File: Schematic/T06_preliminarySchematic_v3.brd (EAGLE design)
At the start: 100 x 80 mm, 58 parts, among them Q3 2n3904, U1 ATMEGA328P_PDIP, X1 SSW-105-02-S-S, X2 SSW-102-02-S-S

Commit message: still trying to figutr out git
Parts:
- CSTCE16M0V53-R0: device adafruit:CERM_OSC -> adafruit:CSTCR-G
- moved SONAR2 120.9 mm to (49.5, 39.4), turned to 270 degrees
- moved R7 117.4 mm to (27.9, 2.54), turned to 270 degrees
- moved SONAR1 111.2 mm to (54.6, 39.4), turned to 270 degrees
- moved TP26 111.1 mm to (24.1, 8.89), turned to 90 degrees
- moved MOTOR2 109.8 mm to (52.1, 74.9), turned to 270 degrees
- moved R2 107.1 mm to (41.9, 3.81), turned to 90 degrees
- moved R1 106.7 mm to (29.2, 47.0)
- moved NCP1117DT33T5GOSTR-ND 105.9 mm to (33.0, 20.3)
- moved TP27 105.5 mm to (38.1, 74.9), turned to 90 degrees
- moved R5 103.1 mm to (40.6, 69.8), turned to 270 degrees
- moved TP15 99.9 mm to (27.9, 59.7), turned to 180 degrees
- moved TP16 99.5 mm to (22.9, 63.5), turned to 270 degrees
- moved MOTOR1 95.8 mm to (45.7, 74.9), turned to 270 degrees
- moved LED3 95.6 mm to (21.6, 2.54)
- moved TP2 95.2 mm to (3.81, 29.2), turned to 90 degrees
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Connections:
- net GND: now also CSTCE16M0V53-R0.2; no longer CSTCE16M0V53-R0.P$2
- net N$1: now also CSTCE16M0V53-R0.3; no longer CSTCE16M0V53-R0.P$3
- net N$2: now also CSTCE16M0V53-R0.1; no longer CSTCE16M0V53-R0.P$1

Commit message: practice makes perfect
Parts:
- removed MOTOR1, MOTOR2: SSW-102-02-S-S, con-samtec:SSW-102-02-S-S
- removed SONAR1, SONAR3: SSW-104-02-S-S, con-samtec:SSW-104-02-S-S
- removed TP15: TPPAD1-13, testpad:P1-13
- added M1, M2: SSW-102-02-S-S, con-samtec:SSW-102-02-S-S
- added S1, S3: SSW-104-02-S-S, con-samtec:SSW-104-02-S-S
- moved R5 7.62 mm to (33.0, 69.8)
- moved TP10 4.58 mm to (21.6, 29.2)
- moved TP11 4.58 mm to (21.6, 33.0)
- moved TP22 4.58 mm to (21.6, 40.6)
- moved TP7 4.58 mm to (21.6, 17.8)
- moved TP8 4.58 mm to (21.6, 21.6)
- moved TP9 4.58 mm to (21.6, 25.4)
- moved TP24 4.58 mm to (21.6, 36.8)
- moved R3 3.70 mm to (21.0, 73.0)
- moved LED2 3.42 mm to (16.5, 73.0)
- moved LED1 3.24 mm to (12.1, 73.0)
- moved TP23 3.24 mm to (3.17, 75.6), turned to 180 degrees
- moved TP26 2.69 mm to (22.2, 10.8)
- moved TP18 2.54 mm to (3.81, 66.0), turned to 180 degrees
- moved X2 2.54 mm to (12.7, 5.08)
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- renumbered CSTCE16M0V53-R0 to CSC, SONAR2 to S2
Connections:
- net +5V: now also S1.4, S3.4; no longer SONAR1.4, SONAR3.4
- net ECHO1: now also S1.2; no longer SONAR1.2
- net ECHO3: now also S3.2; no longer SONAR3.2, TP15.TP
- net GND: now also S1.1, S3.1; no longer SONAR1.1, SONAR3.1
- net N$11: now also M1.2, M2.2; no longer MOTOR1.2, MOTOR2.2
- net N$5: now also M1.1, M2.1; no longer MOTOR1.1, MOTOR2.1
- net TRIG: now also S1.3, S3.3; no longer SONAR1.3, SONAR3.3

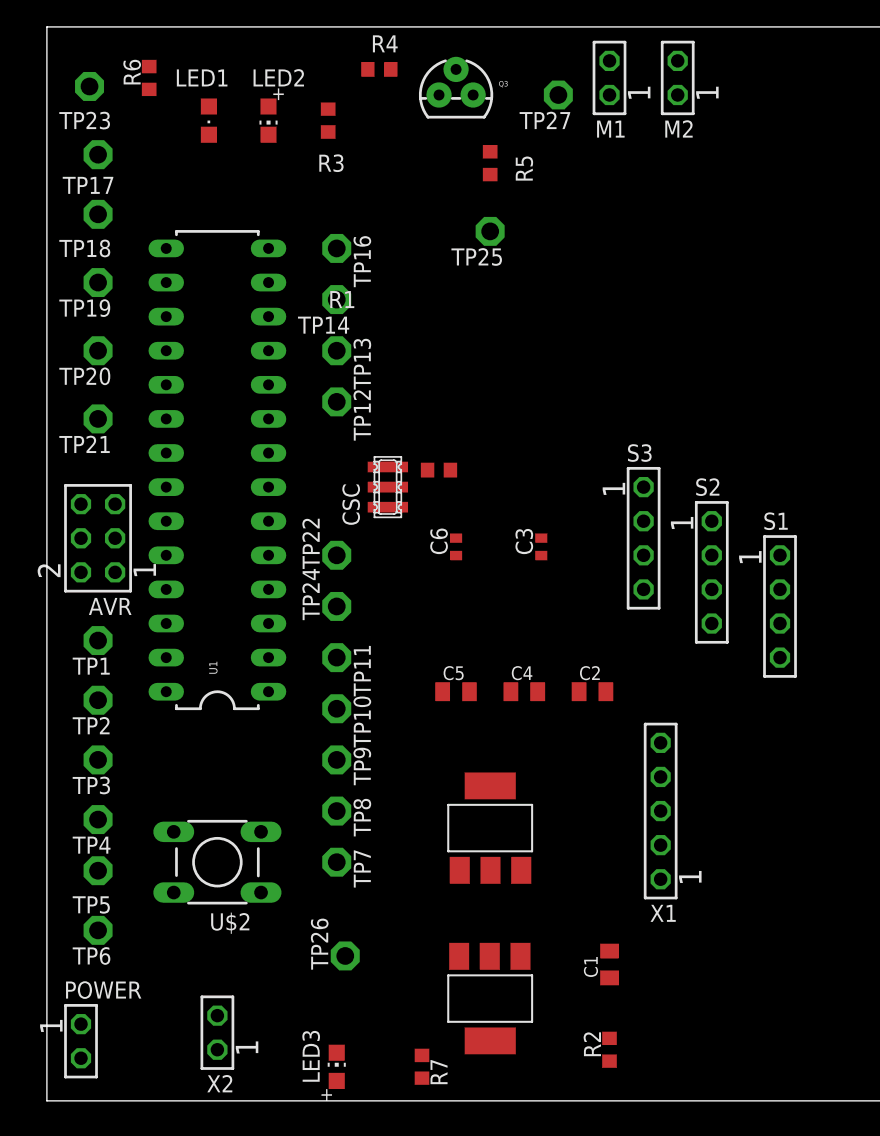
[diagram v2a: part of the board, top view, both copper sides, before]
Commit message: board done and routed, managed to do with only 1 via and no air wires
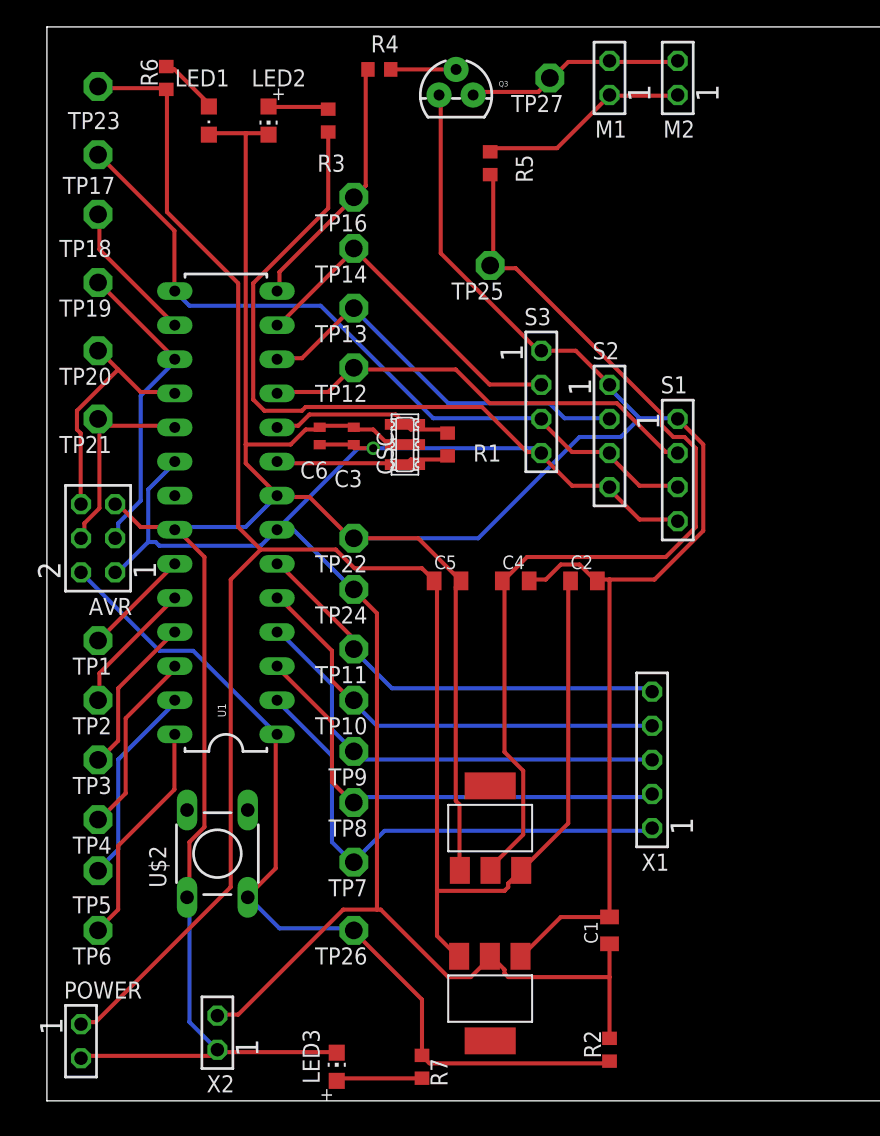
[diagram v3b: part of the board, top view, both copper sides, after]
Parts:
- moved C3 16.2 mm to (22.9, 49.5)
- moved C6 13.1 mm to (20.3, 49.5)
- moved S2 12.7 mm to (41.9, 49.5)
- moved S3 12.7 mm to (36.8, 52.1)
- moved S1 12.7 mm to (47.0, 47.0)
- moved C2 8.28 mm to (40.0, 38.7)
- moved C4 8.28 mm to (34.9, 38.7)
- moved C5 8.28 mm to (29.8, 38.7)
- moved TP14 4.02 mm to (22.9, 63.5)
- moved TP16 4.02 mm to (22.9, 67.3), turned to 180 degrees
- moved X1 3.86 mm to (45.1, 25.4)
- moved CSC 3.42 mm to (26.7, 48.9)
- moved TP13 3.42 mm to (22.9, 59.1), turned to 180 degrees
- moved U1 3.24 mm to (13.3, 43.8)
- moved TP12 2.84 mm to (22.9, 54.6), turned to 180 degrees
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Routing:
- net GND: track 0.00 -> 275.7 mm
- net +5V: track 0.00 -> 180.6 mm, vias 0 -> 1
- net +9V: track 0.00 -> 156.6 mm
- net +3V3: track 0.00 -> 73.7 mm
- net RESET: track 0.00 -> 67.3 mm
- net TRIG: track 0.00 -> 56.3 mm
- net BU0: track 0.00 -> 37.8 mm
- net BU1: track 0.00 -> 35.1 mm
- net BU2: track 0.00 -> 33.8 mm
- net ECHO1: track 0.00 -> 33.3 mm
- net BU3: track 0.00 -> 33.3 mm
- net BU4: track 0.00 -> 32.4 mm
- net ECHO2: track 0.00 -> 29.8 mm
- net ECHO3: track 0.00 -> 26.3 mm
- net MOSI: track 0.00 -> 23.4 mm
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
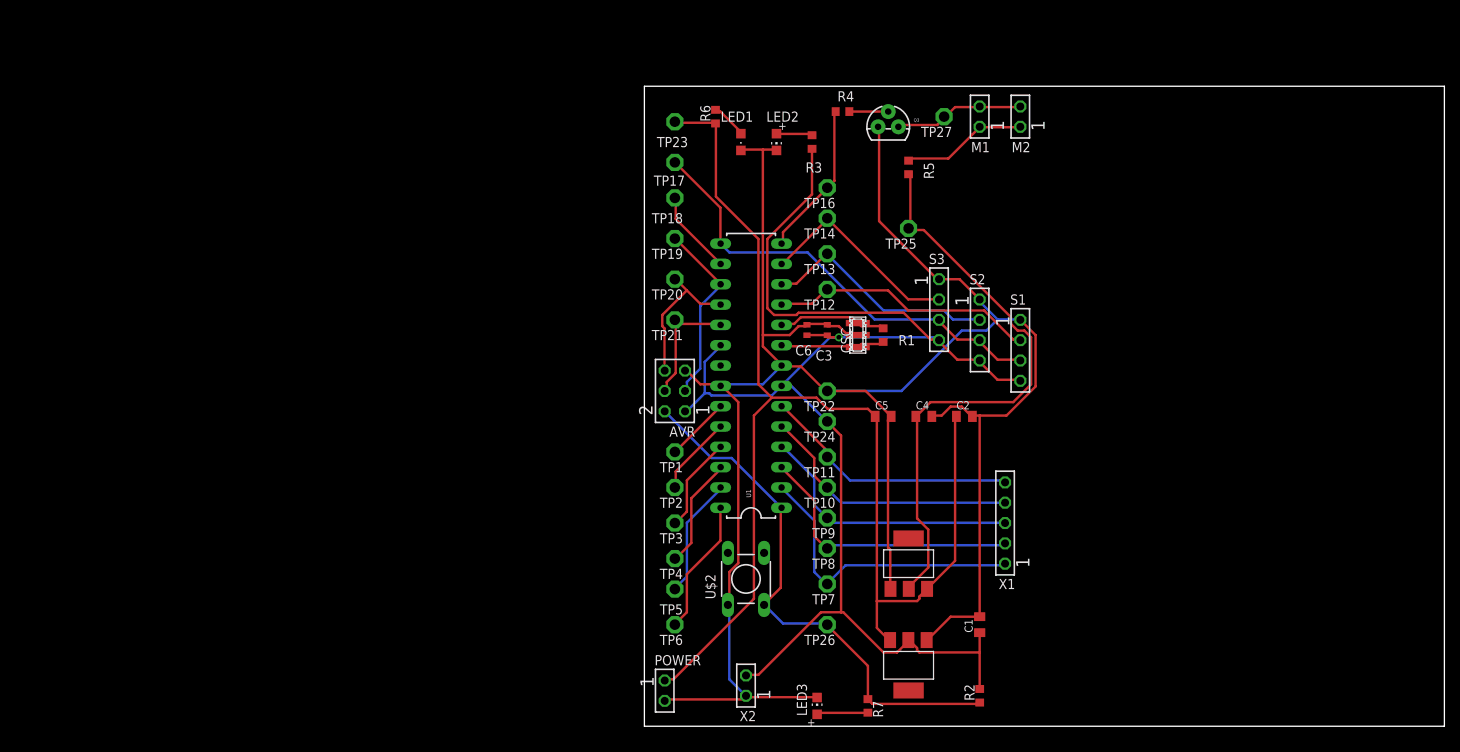
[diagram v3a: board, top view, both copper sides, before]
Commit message: final design with no drc errors finished
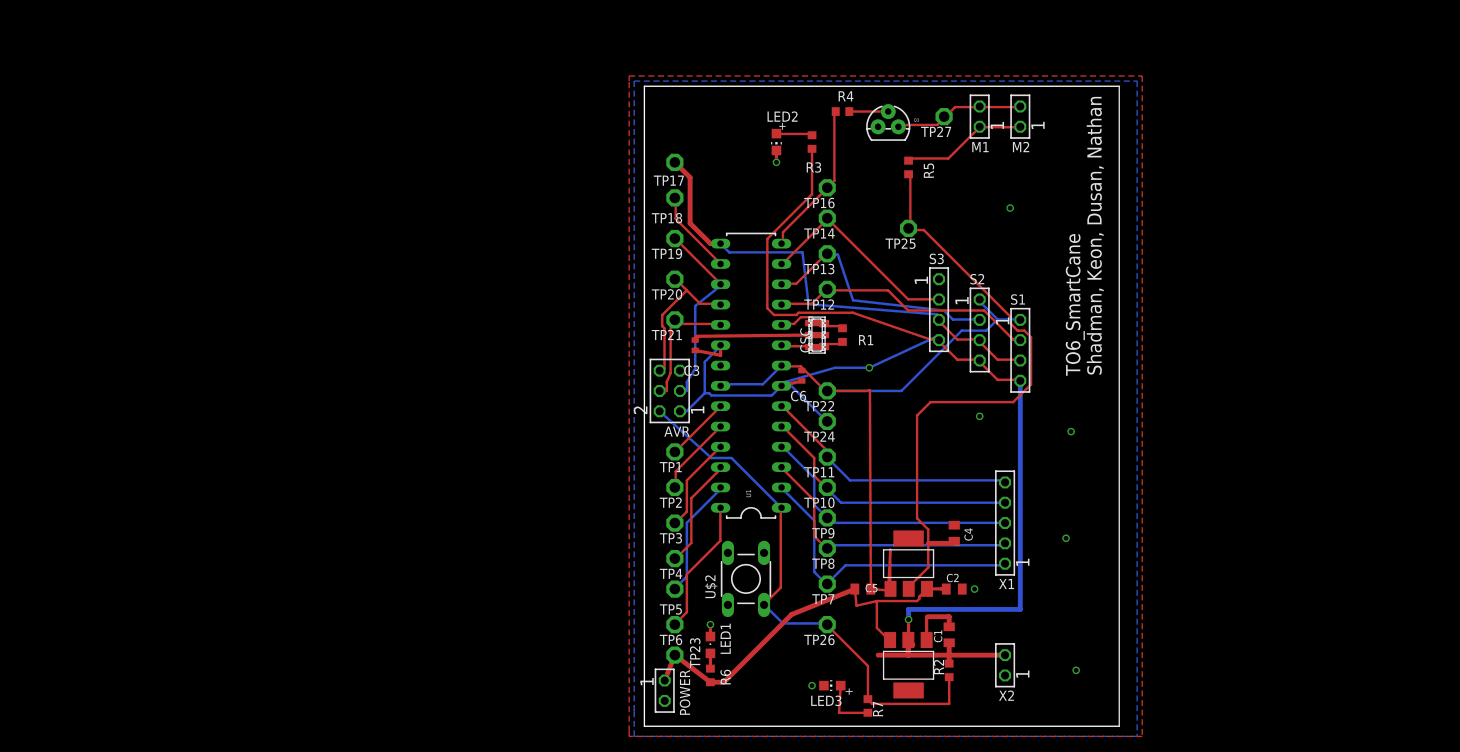
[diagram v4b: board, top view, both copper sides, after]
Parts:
- moved R6 69.9 mm to (8.26, 6.35)
- moved TP23 66.7 mm to (3.81, 8.89)
- moved LED1 63.0 mm to (8.26, 10.2), turned to 0 degrees
- moved X2 32.5 mm to (45.1, 7.62)
- moved C5 21.7 mm to (27.3, 17.1)
- moved C2 21.6 mm to (38.7, 17.1)
- moved C3 16.6 mm to (6.35, 47.6)
- moved C4 15.1 mm to (38.7, 24.1), turned to 90 degrees
- moved C6 5.75 mm to (19.7, 43.8)
- moved CSC 5.08 mm to (21.6, 48.9)
- moved R1 5.08 mm to (24.8, 48.9)
- moved R2 4.96 mm to (38.1, 6.99)
- moved C1 4.02 mm to (38.1, 11.4)
- moved LED3 3.18 mm to (23.5, 5.08), turned to 90 degrees
- moved AVR 0.64 mm to (3.17, 41.9)
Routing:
- net GND: track 275.7 -> 117.2 mm, vias 0 -> 9
- net +9V: track 156.6 -> 51.0 mm
- net N$2: track 13.0 -> 7.97 mm
- net N$1: track 13.7 -> 8.60 mm
- net +5V: track 180.6 -> 184.9 mm, vias 1 -> 2
- net TRIG: track 56.3 -> 60.0 mm
- net +3V3: track 73.7 -> 76.9 mm
- net N$7: track 4.59 -> 1.91 mm
- net ECHO2: track 29.8 -> 31.0 mm
- net SCK: track 15.5 -> 16.6 mm
- net MOSI: track 23.4 -> 24.1 mm
- net N$9: track 6.44 -> 7.03 mm
- added copper zone on layer 1, net GND
- added copper zone on layer 16, net GND
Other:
- board size 100 x 80 mm -> 59.4 x 80 mm
- board text added: "TO6_SmartCane Shadman, Keon, Dusan, Nathan"
